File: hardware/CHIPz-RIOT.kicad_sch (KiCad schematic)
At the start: 37 parts, among them J1 Conn_01x10, Q1 BC847W, Q2 FDN340P, U1 NCP115AMX120TCG, U2 ICE40UP5K-SG48ITR, U3 AT25SF081BMAH*T

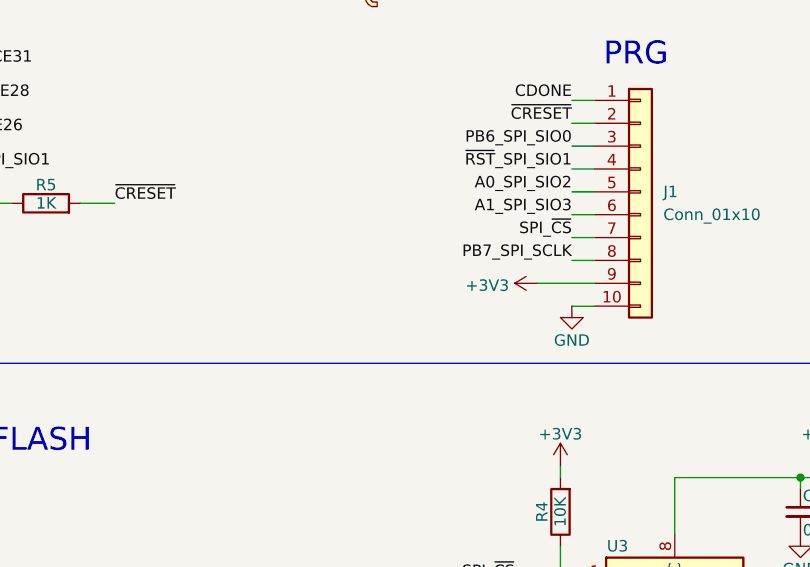
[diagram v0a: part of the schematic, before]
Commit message: Added assembly note/change.
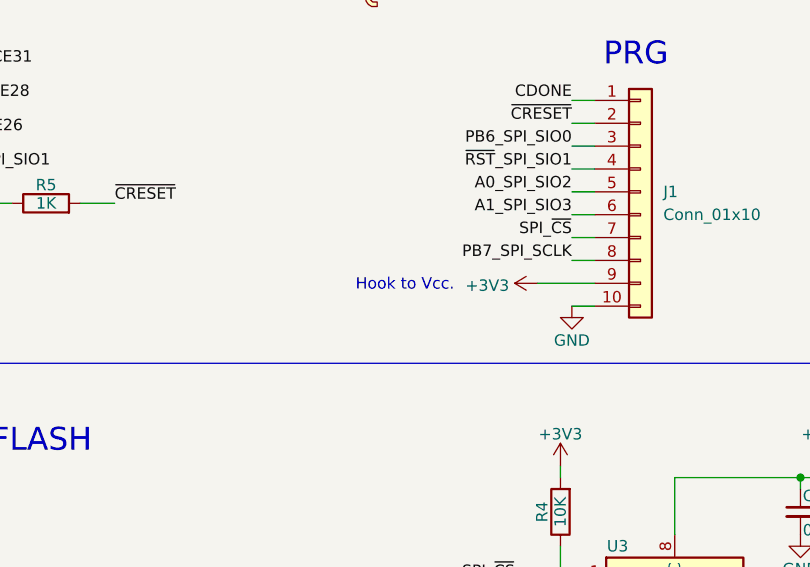
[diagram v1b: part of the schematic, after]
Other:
- note added: "Hook to Vcc."
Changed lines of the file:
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@@
+		)
+	)
+	(text "Hook to Vcc.\n"
+		(exclude_from_sim no)
+		(at 229.108 101.854 0)
+		(effects
+			(font
+				(size 1.27 1.27)
+			)
 		)
 	)
